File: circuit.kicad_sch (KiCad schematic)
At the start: 27 parts, among them SW101 Pedal_1, SW102 Pedal_6, SW103 Pedal_2, SW104 Pedal_7, SW105 Pedal_3, SW106 Pedal_8, SW107 Pedal_4, SW108 Program, SW109 Pedal_5, SW110 Preset, U101 ESP32-S3-DevKitC

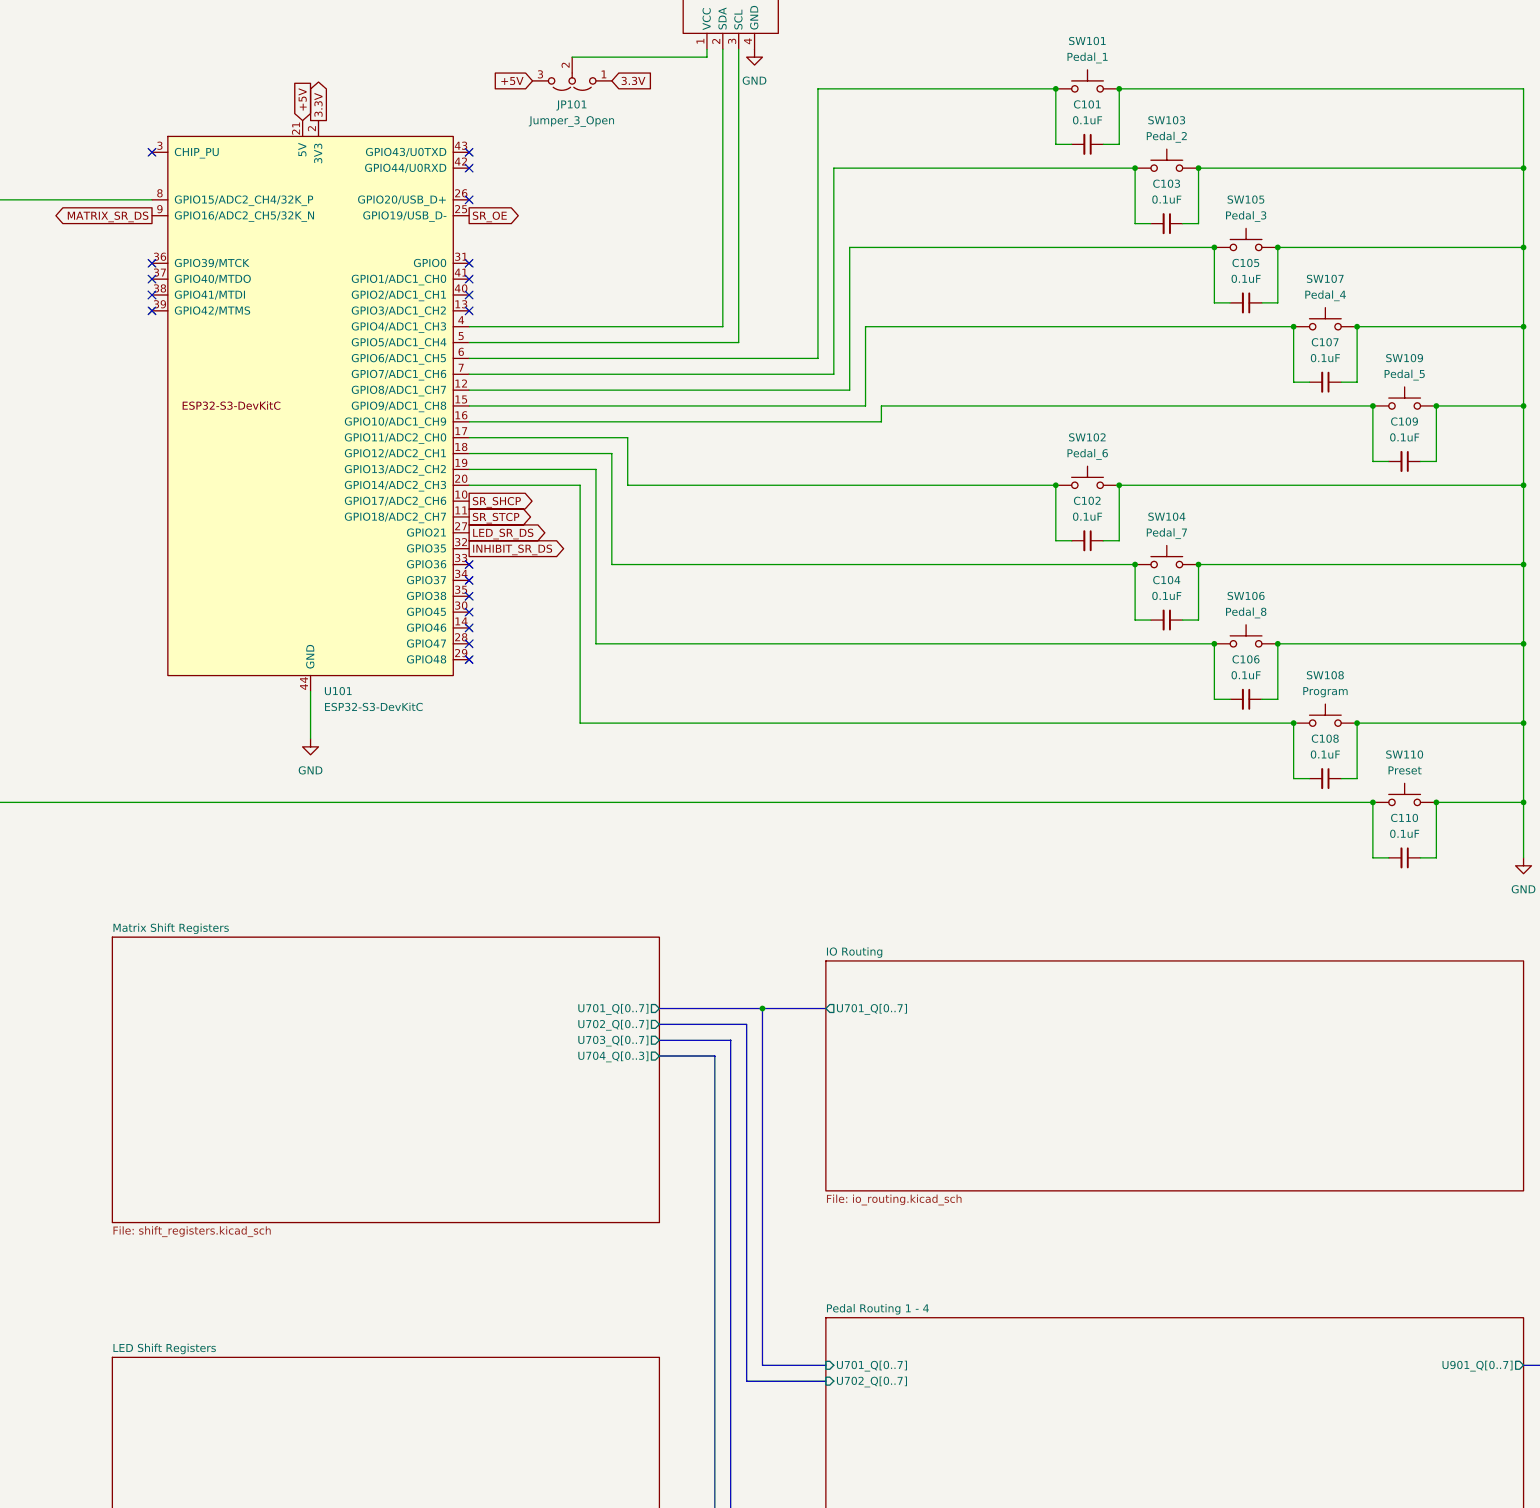
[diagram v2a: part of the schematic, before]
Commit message: Removed LED Shift registers and replaced them with PCA9685 PWM controllers, Also changed LEDs to RGB LEDs.
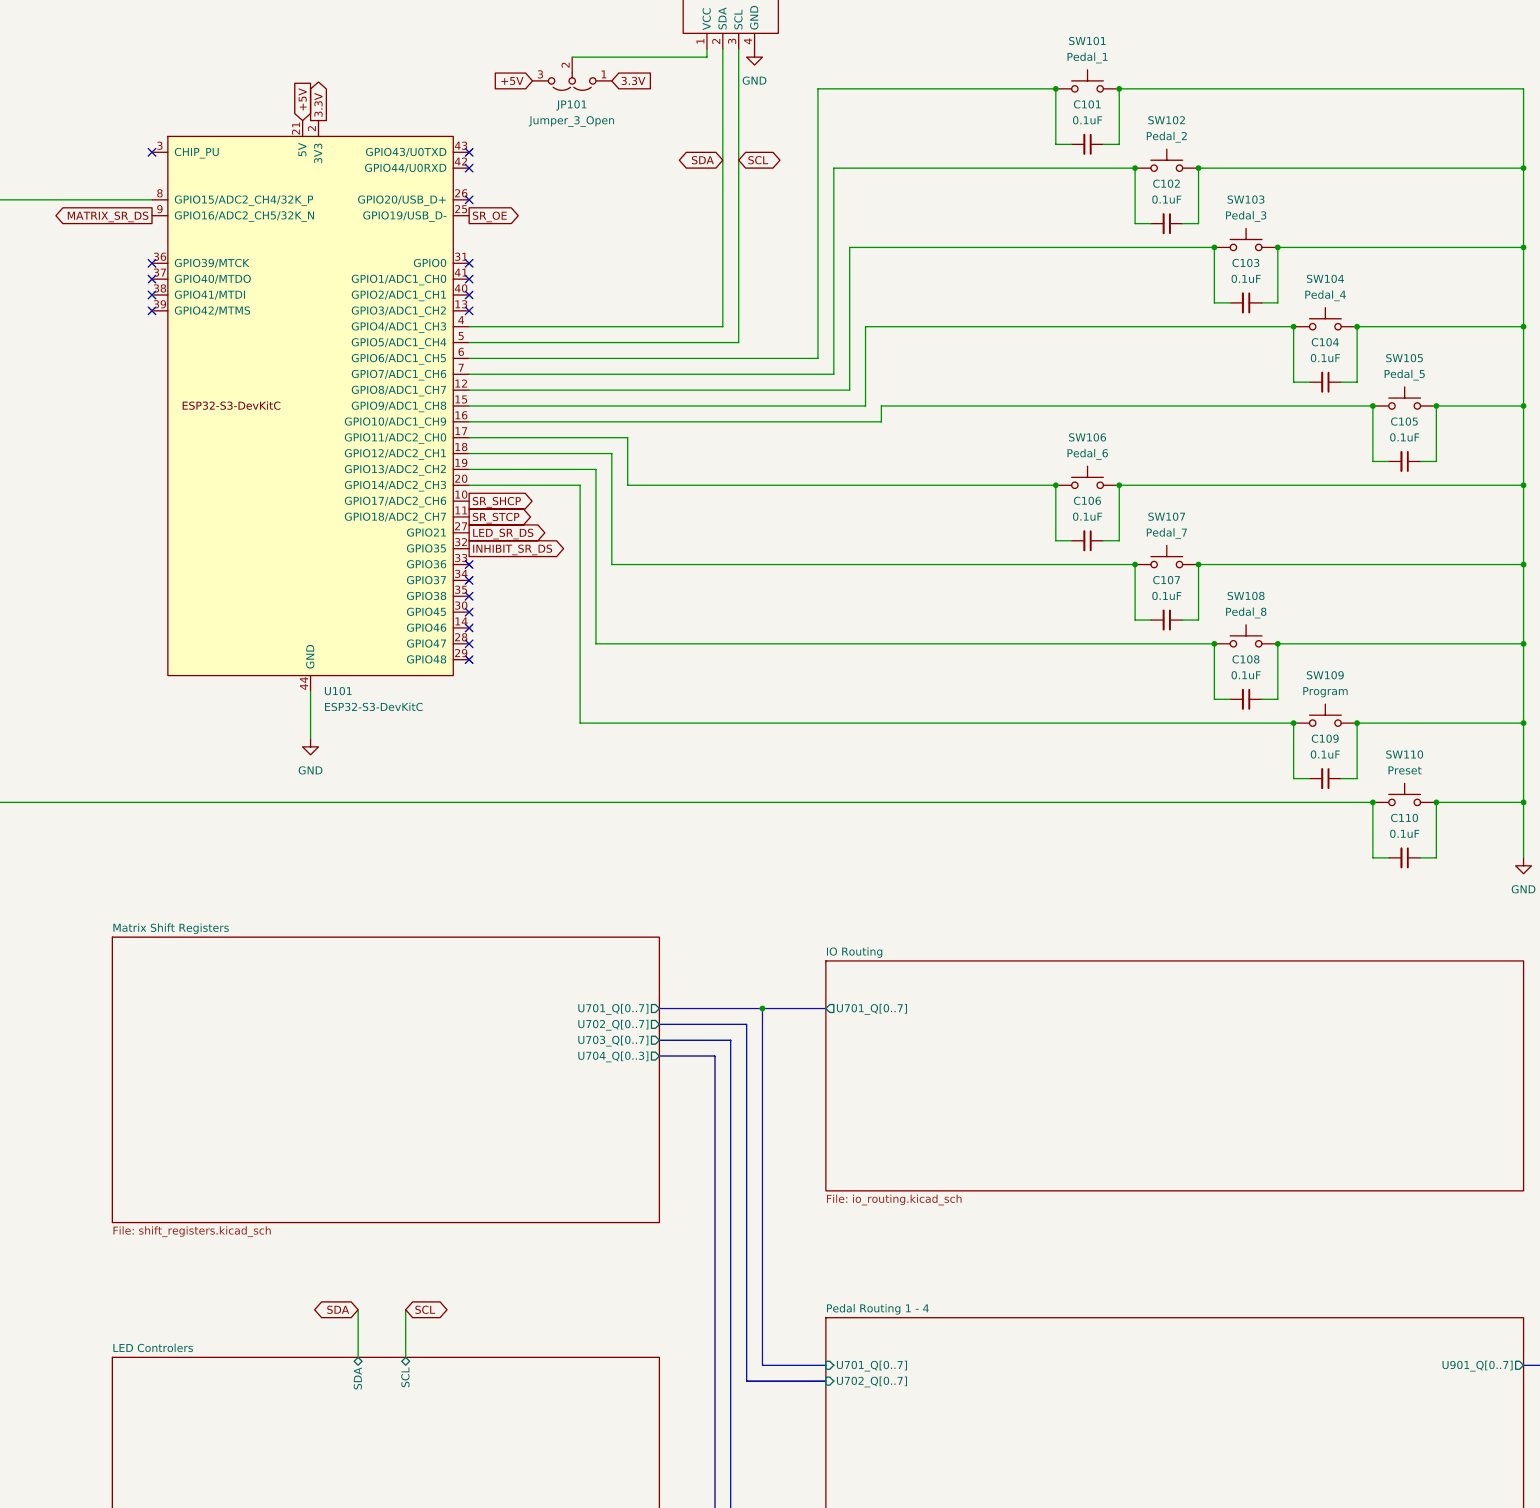
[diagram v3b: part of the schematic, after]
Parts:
- renumbered C103 to C102, C105 to C103, C107 to C104, C109 to C105, C102 to C106, C104 to C107, C106 to C108, C108 to C109, SW103 to SW102, SW105 to SW103, SW107 to SW104, SW109 to SW105, SW102 to SW106, SW104 to SW107, SW106 to SW108, SW108 to SW109
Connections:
- net SDA: now reaches Disp101.2 (SDA), U101.4 (GPIO4/ADC1_CH3)
- net SCL: now reaches Disp101.3 (SCL), U101.5 (GPIO5/ADC1_CH4)
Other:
- sheet LED Shift Registers renamed LED Controlers
- sheet LED Controlers ports: added SCL, SDA; removed none
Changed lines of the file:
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@@
 	(wire
 		(pts
+			(xy 170.18 246.38) (xy 170.18 254)
+		)
+		(stroke
+			(width 0)
+			(type default)
+		)
+	)
+	(wire
+		(pts
 			(xy 299.72 85.09) (xy 299.72 76.2)
 		)
@@
 	(wire
 		(pts
+			(xy 162.56 246.38) (xy 162.56 254)
+		)
+		(stroke
+			(width 0)
+			(type default)
+		)
+	)
+	(wire
+		(pts
 			(xy 243.84 101.6) (xy 180.34 101.6)
 		)
@@
 		)
 	)
+	(global_label "SCL"
+		(shape bidirectional)
+		(at 223.52 62.23 0)
+		(fields_autoplaced yes)
+		(effects
+			(font
+				(size 1.27 1.27)
+			)
+			(justify left)
+		)
+		(property "Intersheetrefs" "${INTERSHEET_REFS}"
+			(at 231.1241 62.23 0)
+			(effects
+				(font
+					(size 1.27 1.27)
+				)
+				(justify left)
+				(hide yes)
+			)
+		)
+	)
 	(global_label "LED_SR_DS"
 		(shape output)
@@
 		)
 	)
+	(global_label "SCL"
+		(shape bidirectional)
+		(at 170.18 246.38 0)
+		(fields_autoplaced yes)
+		(effects
+			(font
+				(size 1.27 1.27)
+			)
+			(justify left)
+		)
+		(property "Intersheetrefs" "${INTERSHEET_REFS}"
+			(at 177.7841 246.38 0)
+			(effects
+				(font
+					(size 1.27 1.27)
+				)
+				(justify left)
+				(hide yes)
+			)
+		)
+	)
 	(global_label "MATRIX_SR_DS"
 		(shape output)
@@
 		)
 	)
+	(global_label "SDA"
+		(shape bidirectional)
+		(at 220.98 62.23 180)
+		(fields_autoplaced yes)
+		(effects
+			(font
+				(size 1.27 1.27)
+			)
+			(justify right)
+		)
+		(property "Intersheetrefs" "${INTERSHEET_REFS}"
+			(at 213.3154 62.23 0)
+			(effects
+				(font
+					(size 1.27 1.27)
+				)
+				(justify right)
+				(hide yes)
+			)
+		)
+	)
+	(global_label "SDA"
+		(shape bidirectional)
+		(at 162.56 246.38 180)
+		(fields_autoplaced yes)
+		(effects
+			(font
+				(size 1.27 1.27)
+			)
+			(justify right)
+		)
+		(property "Intersheetrefs" "${INTERSHEET_REFS}"
+			(at 154.8954 246.38 0)
+			(effects
+				(font
+					(size 1.27 1.27)
+				)
+				(justify right)
+				(hide yes)
+			)
+		)
+	)
 	(global_label "+5V"
 		(shape input)
@@
 		(dnp no)
 		(fields_autoplaced yes)
-		(property "Reference" "SW105"
+		(property "Reference" "SW103"
 			(at 304.8 68.58 0)
 			(effects
@@
 			(project "bay"
 				(path "/420e3d7a-6c9a-4806-b4be-05d56aeb21de"
-					(reference "SW105")
+					(reference "SW103")
 					(unit 1)
 				)
@@
 		(on_board yes)
 		(dnp no)
-		(property "Reference" "C109"
+		(property "Reference" "C105"
 			(at 330.1936 104.14 90)
 			(effects
@@
 			(project "circuit"
 				(path "/420e3d7a-6c9a-4806-b4be-05d56aeb21de"
-					(reference "C109")
+					(reference "C105")
 					(unit 1)
 				)
@@
 		(on_board yes)
 		(dnp no)
-		(property "Reference" "C104"
+		(property "Reference" "C107"
 			(at 292.0936 129.54 90)
 			(effects
@@
 			(project "circuit"
 				(path "/420e3d7a-6c9a-4806-b4be-05d56aeb21de"
-					(reference "C104")
+					(reference "C107")
 					(unit 1)
 				)
@@
 		(dnp no)
 		(fields_autoplaced yes)
-		(property "Reference" "SW102"
+		(property "Reference" "SW106"
 			(at 279.4 106.68 0)
 			(effects
@@
 			(project "bay"
 				(path "/420e3d7a-6c9a-4806-b4be-05d56aeb21de"
-					(reference "SW102")
+					(reference "SW106")
 					(unit 1)
 				)
@@
 		(on_board yes)
 		(dnp no)
-		(property "Reference" "SW109"
+		(property "Reference" "SW105"
 			(at 330.2 93.98 0)
 			(effects
@@
 			(project "bay"
 				(path "/420e3d7a-6c9a-4806-b4be-05d56aeb21de"
-					(reference "SW109")
+					(reference "SW105")
 					(unit 1)
 				)
@@
 		(on_board yes)
 		(dnp no)
-		(property "Reference" "C102"
+		(property "Reference" "C106"
 			(at 279.3936 116.84 90)
 			(effects
@@
 			(project "circuit"
 				(path "/420e3d7a-6c9a-4806-b4be-05d56aeb21de"
-					(reference "C102")
+					(reference "C106")
 					(unit 1)
 				)
@@
 		(dnp no)
 		(fields_autoplaced yes)
-		(property "Reference" "SW108"
+		(property "Reference" "SW109"
 			(at 317.5 144.78 0)
 			(effects
@@
 			(project "bay"
 				(path "/420e3d7a-6c9a-4806-b4be-05d56aeb21de"
-					(reference "SW108")
+					(reference "SW109")
 					(unit 1)
 				)
@@
 		(on_board yes)
 		(dnp no)
-		(property "Reference" "C105"
+		(property "Reference" "C103"
 			(at 304.7936 78.74 90)
 			(effects
@@
 			(project "circuit"
 				(path "/420e3d7a-6c9a-4806-b4be-05d56aeb21de"
-					(reference "C105")
+					(reference "C103")
 					(unit 1)
 				)
@@
 		(dnp no)
 		(fields_autoplaced yes)
-		(property "Reference" "#PWR0104"
+		(property "Reference" "#PWR0106"
 			(at 349.25 180.34 0)
 			(effects
@@
 			(project "circuit"
 				(path "/420e3d7a-6c9a-4806-b4be-05d56aeb21de"
-					(reference "#PWR0104")
+					(reference "#PWR0106")
 					(unit 1)
 				)
@@
 		(dnp no)
 		(fields_autoplaced yes)
-		(property "Reference" "SW103"
+		(property "Reference" "SW102"
 			(at 292.1 55.88 0)
 			(effects
@@
 			(project "bay"
 				(path "/420e3d7a-6c9a-4806-b4be-05d56aeb21de"
-					(reference "SW103")
+					(reference "SW102")
 					(unit 1)
 				)
@@
 		(dnp no)
 		(fields_autoplaced yes)
-		(property "Reference" "SW106"
+		(property "Reference" "SW108"
 			(at 304.8 132.08 0)
 			(effects
@@
 			(project "bay"
 				(path "/420e3d7a-6c9a-4806-b4be-05d56aeb21de"
-					(reference "SW106")
+					(reference "SW108")
 					(unit 1)
 				)
@@
 		(dnp no)
 		(fields_autoplaced yes)
-		(property "Reference" "#PWR0105"
+		(property "Reference" "#PWR0101"
 			(at 375.92 44.45 0)
 			(effects
@@
 			(project ""
 				(path "/420e3d7a-6c9a-4806-b4be-05d56aeb21de"
-					(reference "#PWR0105")
+					(reference "#PWR0101")
 					(unit 1)
 				)
@@
 		(on_board yes)
 		(dnp no)
-		(property "Reference" "C108"
+		(property "Reference" "C109"
 			(at 317.4936 154.94 90)
 			(effects
@@
 			(project "circuit"
 				(path "/420e3d7a-6c9a-4806-b4be-05d56aeb21de"
-					(reference "C108")
+					(reference "C109")
 					(unit 1)
 				)
@@
 		(on_board yes)
 		(dnp no)
-		(property "Reference" "C106"
+		(property "Reference" "C108"
 			(at 304.7936 142.24 90)
 			(effects
@@
 			(project "circuit"
 				(path "/420e3d7a-6c9a-4806-b4be-05d56aeb21de"
-					(reference "C106")
+					(reference "C108")
 					(unit 1)
 				)
@@
 		(dnp no)
 		(fields_autoplaced yes)
-		(property "Reference" "SW107"
+		(property "Reference" "SW104"
 			(at 317.5 81.28 0)
 			(effects
@@
 			(project "bay"
 				(path "/420e3d7a-6c9a-4806-b4be-05d56aeb21de"
-					(reference "SW107")
+					(reference "SW104")
 					(unit 1)
 				)
@@
 		(dnp no)
 		(fields_autoplaced yes)
-		(property "Reference" "#PWR0101"
+		(property "Reference" "#PWR0104"
 			(at 30.48 77.47 0)
 			(effects
@@
 			(project ""
 				(path "/420e3d7a-6c9a-4806-b4be-05d56aeb21de"
-					(reference "#PWR0101")
+					(reference "#PWR0104")
 					(unit 1)
 				)
@@
 		(on_board yes)
 		(dnp no)
-		(property "Reference" "C107"
+		(property "Reference" "C104"
 			(at 317.4936 91.44 90)
 			(effects
@@
 			(project "circuit"
 				(path "/420e3d7a-6c9a-4806-b4be-05d56aeb21de"
-					(reference "C107")
+					(reference "C104")
 					(unit 1)
 				)
@@
 		(dnp no)
 		(fields_autoplaced yes)
-		(property "Reference" "#PWR0106"
+		(property "Reference" "#PWR0102"
 			(at 386.08 44.45 0)
 			(effects
@@
 			(project "circuit"
 				(path "/420e3d7a-6c9a-4806-b4be-05d56aeb21de"
-					(reference "#PWR0106")
+					(reference "#PWR0102")
 					(unit 1)
 				)
@@
 		(on_board yes)
 		(dnp no)
-		(property "Reference" "C103"
+		(property "Reference" "C102"
 			(at 292.0936 66.04 90)
 			(effects
@@
 			(project "circuit"
 				(path "/420e3d7a-6c9a-4806-b4be-05d56aeb21de"
-					(reference "C103")
+					(reference "C102")
 					(unit 1)
 				)
@@
 		(on_board yes)
 		(dnp no)
-		(property "Reference" "SW104"
+		(property "Reference" "SW107"
 			(at 292.1 119.38 0)
 			(effects
@@
 			(project "bay"
 				(path "/420e3d7a-6c9a-4806-b4be-05d56aeb21de"
-					(reference "SW104")
+					(reference "SW107")
 					(unit 1)
 				)
@@
 		(dnp no)
 		(fields_autoplaced yes)
-		(property "Reference" "#PWR0102"
+		(property "Reference" "#PWR0105"
 			(at 154.94 161.29 0)
 			(effects
@@
 			(project ""
 				(path "/420e3d7a-6c9a-4806-b4be-05d56aeb21de"
-					(reference "#PWR0102")
+					(reference "#PWR0105")
 					(unit 1)
 				)
@@
 			(color 0 0 0 0.0000)
 		)
-		(property "Sheetname" "LED Shift Registers"
+		(property "Sheetname" "LED Controlers"
 			(at 123.19 253.2884 0)
 			(effects
@@
 			)
 		)
+		(pin "SCL" bidirectional
+			(at 170.18 254 90)
+			(effects
+				(font
+					(size 1.27 1.27)
+				)
+				(justify right)
+			)
+		)
+		(pin "SDA" bidirectional
+			(at 162.56 254 90)
+			(effects
+				(font
+					(size 1.27 1.27)
+				)
+				(justify right)
+			)
+		)
